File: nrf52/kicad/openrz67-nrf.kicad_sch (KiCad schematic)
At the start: 13 parts, among them J1 Camera, J2 SWD, SW1 B3U-1000P, U1 E73-2G4M08S1C, U2 TLP172AM, U3 TLP172AM

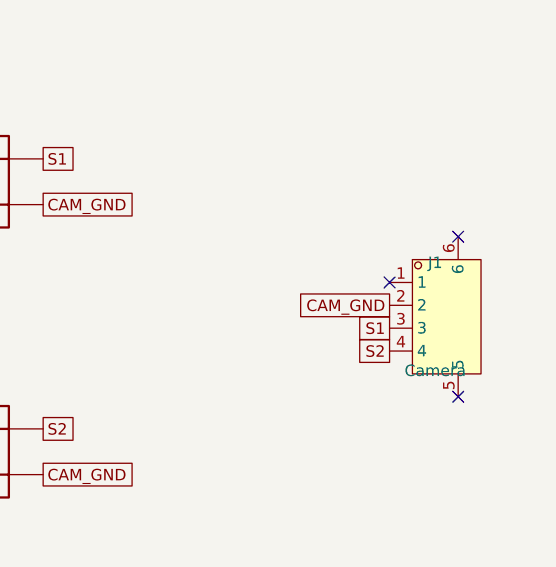
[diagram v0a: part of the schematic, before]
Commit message: nrf52: JST SH camera connector, datasheet facts
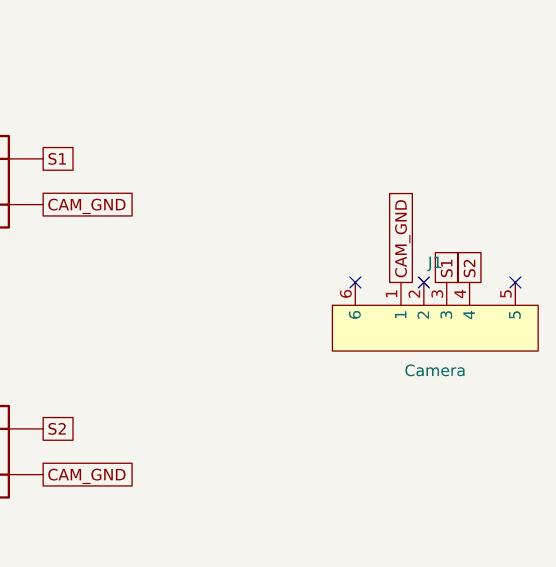
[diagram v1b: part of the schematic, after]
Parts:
- removed J1: Camera, openrz67-nrf:CONN-SMD_S4B-XH-SM4-TB-LF-SN, symbol openrz67-nrf:S4B-XH-SM4-TB-
- added J1: Camera, openrz67-nrf:CONN-SMD_4P-P1.00_SM04B-SRSS-TB-LF-SN, symbol openrz67-nrf:SM04B-SRSS-TB
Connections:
- net CAM_GND: now also J1.1
- net S1: now also J1.3
- net S2: now also J1.4
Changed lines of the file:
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@@
     )
   )
-  (symbol (lib_id "openrz67-nrf:S4B-XH-SM4-TB-") (at 230 135 0) (unit 1)
+  (symbol (lib_id "openrz67-nrf:SM04B-SRSS-TB") (at 230 135 0) (unit 1)
     (in_bom yes) (on_board yes) (dnp no)
     (property "Reference" "J1" (at 230 129 0)
@@
       (effects (font (size 1.27 1.27)))
     )
-    (property "Footprint" "openrz67-nrf:CONN-SMD_S4B-XH-SM4-TB-LF-SN" (at 230 135 0)
+    (property "Footprint" "openrz67-nrf:CONN-SMD_4P-P1.00_SM04B-SRSS-TB-LF-SN" (at 230 135 0)
       (effects (font (size 1.27 1.27)) hide)
     )
@@
       (effects (font (size 1.27 1.27)) hide)
     )
-    (property "Description" "XH 2.5 mm side-entry SMD: 1 NC, 2 GND, 3 S1, 4 S2" (at 230 135 0)
-      (effects (font (size 1.27 1.27)) hide)
-    )
-    (property "LCSC" "C161861" (at 230 135 0)
-      (effects (font (size 1.27 1.27)) hide)
-    )
-    (property "MPN" "S4B-XH-SM4-TB(LF)(SN)" (at 230 135 0)
+    (property "Description" "SH 1.0 mm side-entry SMD (Qwiic cable fits): 1 GND, 2 NC, 3 S1, 4 S2" (at 230 135 0)
+      (effects (font (size 1.27 1.27)) hide)
+    )
+    (property "LCSC" "C160404" (at 230 135 0)
+      (effects (font (size 1.27 1.27)) hide)
+    )
+    (property "MPN" "SM04B-SRSS-TB(LF)(SN)" (at 230 135 0)
       (effects (font (size 1.27 1.27)) hide)
     )
@@
     (effects (font (size 1.27 1.27)) (justify right))
   )
-  (global_label "CAM_GND" (shape passive) (at 224.92 133.73 180) (fields_autoplaced yes)
-    (effects (font (size 1.27 1.27)) (justify right))
-  )
-  (global_label "S1" (shape passive) (at 224.92 136.27 180) (fields_autoplaced yes)
-    (effects (font (size 1.27 1.27)) (justify right))
-  )
-  (global_label "S2" (shape passive) (at 224.92 138.81 180) (fields_autoplaced yes)
-    (effects (font (size 1.27 1.27)) (justify right))
+  (global_label "CAM_GND" (shape passive) (at 226.19 131.19 90) (fields_autoplaced yes)
+    (effects (font (size 1.27 1.27)) (justify left))
+  )
+  (global_label "S1" (shape passive) (at 231.27 131.19 90) (fields_autoplaced yes)
+    (effects (font (size 1.27 1.27)) (justify left))
+  )
+  (global_label "S2" (shape passive) (at 233.81 131.19 90) (fields_autoplaced yes)
+    (effects (font (size 1.27 1.27)) (justify left))
   )
   (global_label "S1_LED" (shape passive) (at 163.57 117.46 180) (fields_autoplaced yes)
@@
   (no_connect (at 90.48 73.49))
   (no_connect (at 90.48 68.41))
-  (no_connect (at 224.92 131.19))
-  (no_connect (at 232.54 143.89))
-  (no_connect (at 232.54 126.11))
+  (no_connect (at 228.73 131.19))
+  (no_connect (at 238.89 131.19))
+  (no_connect (at 221.11 131.19))
   (sheet_instances (path "/" (page "1")))
   (embedded_fonts no)

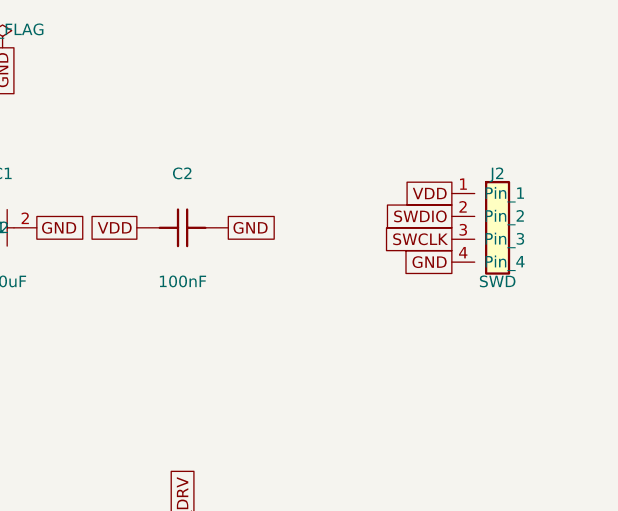
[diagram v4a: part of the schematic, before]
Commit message: nrf52: SH connector for SWD, parts list
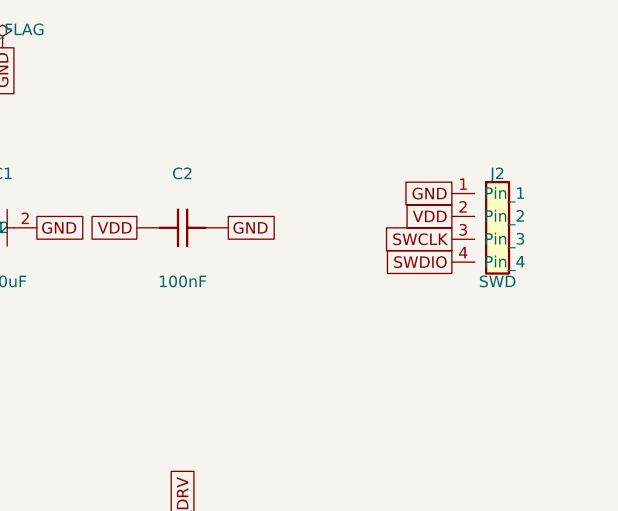
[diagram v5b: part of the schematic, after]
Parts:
- J2: footprint openrz67-nrf:SWD_1x04_P2.54 -> openrz67-nrf:CONN-SMD_4P-P1.00_SM04B-SRSS-TB-LF-SN; LCSC (none) -> C160404; MPN (none) -> SM04B-SRSS-TB(LF)(SN); Manufacturer (none) -> JST; now in the parts list
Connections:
- net GND: now also J2.1 (Pin_1); no longer J2.4 (Pin_4)
- net SWDIO: now also J2.4 (Pin_4); no longer J2.2 (Pin_2)
- net VDD: now also J2.2 (Pin_2); no longer J2.1 (Pin_1)
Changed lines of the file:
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@@
   )
   (symbol (lib_id "openrz67-nrf:Conn_01x04") (at 230 40 0) (unit 1)
-    (in_bom no) (on_board yes) (dnp no)
+    (in_bom yes) (on_board yes) (dnp no)
     (property "Reference" "J2" (at 230 34 0)
       (effects (font (size 1.27 1.27)))
@@
       (effects (font (size 1.27 1.27)))
     )
-    (property "Footprint" "openrz67-nrf:SWD_1x04_P2.54" (at 230 40 0)
+    (property "Footprint" "openrz67-nrf:CONN-SMD_4P-P1.00_SM04B-SRSS-TB-LF-SN" (at 230 40 0)
       (effects (font (size 1.27 1.27)) hide)
     )
@@
       (effects (font (size 1.27 1.27)) hide)
     )
-    (property "Description" "SWD pads: 1 VDD, 2 SWDIO, 3 SWCLK, 4 GND" (at 230 40 0)
-      (effects (font (size 1.27 1.27)) hide)
-    )
-    (property "LCSC" "" (at 230 40 0)
-      (effects (font (size 1.27 1.27)) hide)
-    )
-    (property "MPN" "" (at 230 40 0)
-      (effects (font (size 1.27 1.27)) hide)
-    )
-    (property "Manufacturer" "" (at 230 40 0)
+    (property "Description" "SWD, SH 1.0 mm side-entry (Qwiic cable to the probe): 1 GND, 2 VDD, 3 SWCLK, 4 SWDIO" (at 230 40 0)
+      (effects (font (size 1.27 1.27)) hide)
+    )
+    (property "LCSC" "C160404" (at 230 40 0)
+      (effects (font (size 1.27 1.27)) hide)
+    )
+    (property "MPN" "SM04B-SRSS-TB(LF)(SN)" (at 230 40 0)
+      (effects (font (size 1.27 1.27)) hide)
+    )
+    (property "Manufacturer" "JST" (at 230 40 0)
       (effects (font (size 1.27 1.27)) hide)
     )
@@
     (effects (font (size 1.27 1.27)) (justify left))
   )
-  (global_label "VDD" (shape passive) (at 224.92 36.19 180) (fields_autoplaced yes)
-    (effects (font (size 1.27 1.27)) (justify right))
-  )
-  (global_label "SWDIO" (shape passive) (at 224.92 38.73 180) (fields_autoplaced yes)
+  (global_label "GND" (shape passive) (at 224.92 36.19 180) (fields_autoplaced yes)
+    (effects (font (size 1.27 1.27)) (justify right))
+  )
+  (global_label "VDD" (shape passive) (at 224.92 38.73 180) (fields_autoplaced yes)
     (effects (font (size 1.27 1.27)) (justify right))
   )
@@
     (effects (font (size 1.27 1.27)) (justify right))
   )
-  (global_label "GND" (shape passive) (at 224.92 43.81 180) (fields_autoplaced yes)
-    (effects (font (size 1.27 1.27)) (justify right))
-  )
+  (global_label "SWDIO" (shape passive) (at 224.92 43.81 180) (fields_autoplaced yes)
+    (effects (font (size 1.27 1.27)) (justify right))
+  )
